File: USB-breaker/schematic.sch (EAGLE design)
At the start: 12 parts, among them K1 G6K-2F-RF, K2 G6K-2F-RF

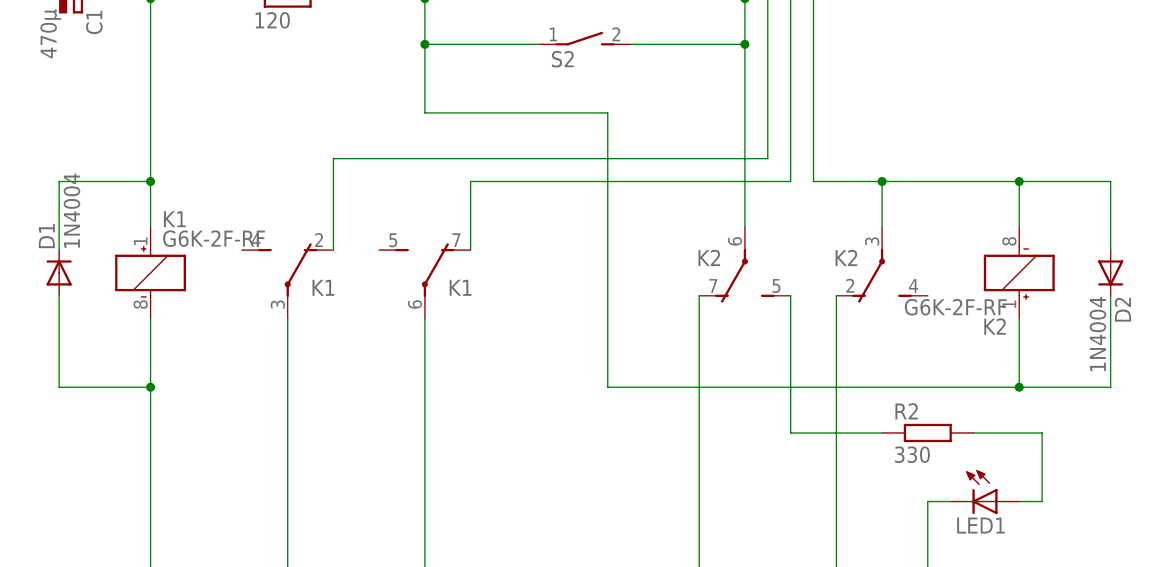
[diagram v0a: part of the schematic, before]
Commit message: Replaced K1 & K2 relay G6K-RF with G6K-2P. SMD --> THT
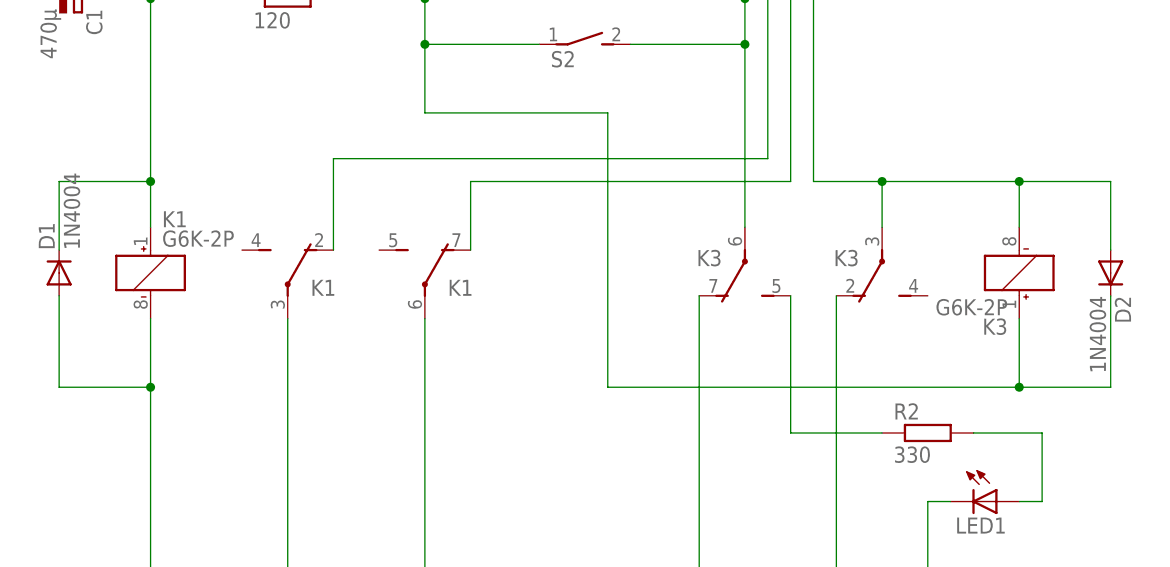
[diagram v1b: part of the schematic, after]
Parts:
- removed K2: G6K-2F-RF, relay:G6K-2F-RF
- added K3: G6K-2P, relay:G6K-2P
- K1: value G6K-2F-RF -> G6K-2P; device relay:G6K-2F-RF -> relay:G6K-2P
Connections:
- net D+-IN: now also K13.O; no longer K1B.O
- net D+-OUT: now also K13.P; no longer K1B.P
- net D--IN: now also K12.O; no longer K1A.O
- net D--OUT: now also K12.P; no longer K1A.P
- net ENABLE: now also K31.+; no longer K21.+
- net GND-IN: now also K31.-, K32.P; no longer K21.-, K2A.P
- net GND-OUT: now also K32.O; no longer K2A.O
- net N$7: now also K33.S; no longer K2B.S
- net VCC-IN: now also K33.P; no longer K2B.P
- net VCC-OUT: now also K33.O; no longer K2B.O
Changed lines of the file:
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@@
 <part name="X1" library="con-berg" deviceset="PN87520" device=""/>
 <part name="X2" library="con-berg" deviceset="PN87520" device=""/>
-<part name="K1" library="relay" deviceset="G6K*-2F-RF" device=""/>
-<part name="K2" library="relay" deviceset="G6K*-2F-RF" device=""/>
 <part name="S1" library="switch-omron" deviceset="31-XX" device=""/>
 <part name="R1" library="resistor" deviceset="R-EU_" device="0207/10" value="120"/>
@@
 <part name="R2" library="resistor" deviceset="R-EU_" device="0207/10" value="330"/>
 <part name="D2" library="diode" deviceset="1N4004" device=""/>
+<part name="K1" library="relay" deviceset="G6K" device="-2P"/>
+<part name="K3" library="relay" deviceset="G6K" device="-2P"/>
 </parts>
 <sheets>
@@
 <instance part="X1" gate="G$1" x="114.3" y="114.3" rot="R90"/>
 <instance part="X2" gate="G$1" x="152.4" y="40.64" rot="MR180"/>
-<instance part="K1" gate="1" x="43.18" y="78.74"/>
-<instance part="K1" gate="A" x="58.42" y="76.2"/>
-<instance part="K1" gate="B" x="73.66" y="76.2"/>
-<instance part="K2" gate="1" x="139.7" y="78.74" rot="R180"/>
-<instance part="K2" gate="A" x="124.46" y="81.28" rot="R180"/>
-<instance part="K2" gate="B" x="109.22" y="81.28" rot="R180"/>
 <instance part="S1" gate="1" x="91.44" y="109.22" rot="R270"/>
 <instance part="R1" gate="G$1" x="58.42" y="109.22"/>
@@
 <instance part="R2" gate="G$1" x="129.54" y="60.96"/>
 <instance part="D2" gate="1" x="149.86" y="78.74" rot="R270"/>
+<instance part="K1" gate="1" x="43.18" y="78.74"/>
+<instance part="K1" gate="2" x="58.42" y="76.2"/>
+<instance part="K1" gate="3" x="73.66" y="76.2"/>
+<instance part="K3" gate="1" x="139.7" y="78.74" rot="R180"/>
+<instance part="K3" gate="2" x="124.46" y="81.28" rot="R180"/>
+<instance part="K3" gate="3" x="109.22" y="81.28" rot="R180"/>
 </instances>
 <busses>
@@
 <wire x1="96.52" y1="109.22" x2="109.22" y2="109.22" width="0.1524" layer="91"/>
 <junction x="109.22" y="109.22"/>
-<pinref part="K2" gate="B" pin="P"/>
 <pinref part="S2" gate="1" pin="2"/>
 <wire x1="96.52" y1="104.14" x2="109.22" y2="104.14" width="0.1524" layer="91"/>
 <junction x="109.22" y="104.14"/>
+<pinref part="K3" gate="3" pin="P"/>
 </segment>
 </net>
@@
 <wire x1="116.84" y1="111.76" x2="116.84" y2="88.9" width="0.1524" layer="91"/>
 <wire x1="116.84" y1="88.9" x2="124.46" y2="88.9" width="0.1524" layer="91"/>
-<pinref part="K2" gate="A" pin="P"/>
 <wire x1="124.46" y1="88.9" x2="124.46" y2="83.82" width="0.1524" layer="91"/>
 <wire x1="124.46" y1="88.9" x2="139.7" y2="88.9" width="0.1524" layer="91"/>
 <junction x="124.46" y="88.9"/>
-<pinref part="K2" gate="1" pin="-"/>
 <wire x1="139.7" y1="88.9" x2="139.7" y2="83.82" width="0.1524" layer="91"/>
 <wire x1="139.7" y1="88.9" x2="149.86" y2="88.9" width="0.1524" layer="91"/>
@@
 <junction x="139.7" y="88.9"/>
 <pinref part="D2" gate="1" pin="A"/>
+<pinref part="K3" gate="1" pin="-"/>
+<pinref part="K3" gate="2" pin="P"/>
 </segment>
 </net>
 <net name="GND-OUT" class="0">
 <segment>
-<pinref part="X2" gate="G$1" pin="4"/>
-<pinref part="K1" gate="1" pin="-"/>
 <wire x1="43.18" y1="73.66" x2="43.18" y2="66.04" width="0.1524" layer="91"/>
 <wire x1="43.18" y1="66.04" x2="43.18" y2="43.18" width="0.1524" layer="91"/>
-<wire x1="43.18" y1="43.18" x2="119.38" y2="43.18" width="0.1524" layer="91"/>
 <pinref part="C1" gate="G$1" pin="-"/>
-<wire x1="119.38" y1="43.18" x2="129.54" y2="43.18" width="0.1524" layer="91"/>
-<wire x1="129.54" y1="43.18" x2="149.86" y2="43.18" width="0.1524" layer="91"/>
 <wire x1="30.48" y1="109.22" x2="25.4" y2="109.22" width="0.1524" layer="91"/>
 <wire x1="25.4" y1="109.22" x2="25.4" y2="43.18" width="0.1524" layer="91"/>
 <wire x1="25.4" y1="43.18" x2="43.18" y2="43.18" width="0.1524" layer="91"/>
-<junction x="43.18" y="43.18"/>
 <pinref part="D1" gate="1" pin="A"/>
 <wire x1="33.02" y1="76.2" x2="33.02" y2="66.04" width="0.1524" layer="91"/>
 <wire x1="33.02" y1="66.04" x2="43.18" y2="66.04" width="0.1524" layer="91"/>
 <junction x="43.18" y="66.04"/>
-<pinref part="K2" gate="A" pin="O"/>
-<wire x1="119.38" y1="76.2" x2="119.38" y2="43.18" width="0.1524" layer="91"/>
-<junction x="119.38" y="43.18"/>
+<pinref part="K1" gate="1" pin="-"/>
+<pinref part="X2" gate="G$1" pin="4"/>
+<wire x1="129.54" y1="43.18" x2="149.86" y2="43.18" width="0.1524" layer="91"/>
 <pinref part="LED1" gate="G$1" pin="C"/>
 <wire x1="132.08" y1="53.34" x2="129.54" y2="53.34" width="0.1524" layer="91"/>
 <wire x1="129.54" y1="53.34" x2="129.54" y2="43.18" width="0.1524" layer="91"/>
 <junction x="129.54" y="43.18"/>
+<wire x1="119.38" y1="43.18" x2="129.54" y2="43.18" width="0.1524" layer="91"/>
+<wire x1="119.38" y1="76.2" x2="119.38" y2="43.18" width="0.1524" layer="91"/>
+<wire x1="43.18" y1="43.18" x2="119.38" y2="43.18" width="0.1524" layer="91"/>
+<junction x="43.18" y="43.18"/>
+<junction x="119.38" y="43.18"/>
+<pinref part="K3" gate="2" pin="O"/>
 </segment>
 </net>
@@
 <pinref part="X2" gate="G$1" pin="1"/>
 <wire x1="104.14" y1="35.56" x2="149.86" y2="35.56" width="0.1524" layer="91"/>
-<pinref part="K2" gate="B" pin="O"/>
 <wire x1="104.14" y1="76.2" x2="104.14" y2="35.56" width="0.1524" layer="91"/>
+<pinref part="K3" gate="3" pin="O"/>
 </segment>
 </net>
@@
 <wire x1="111.76" y1="111.76" x2="111.76" y2="91.44" width="0.1524" layer="91"/>
 <wire x1="111.76" y1="91.44" x2="63.5" y2="91.44" width="0.1524" layer="91"/>
-<pinref part="K1" gate="A" pin="O"/>
+<pinref part="K1" gate="2" pin="O"/>
 <wire x1="63.5" y1="91.44" x2="63.5" y2="81.28" width="0.1524" layer="91"/>
 </segment>
@@
 <wire x1="114.3" y1="111.76" x2="114.3" y2="88.9" width="0.1524" layer="91"/>
 <wire x1="114.3" y1="88.9" x2="78.74" y2="88.9" width="0.1524" layer="91"/>
-<pinref part="K1" gate="B" pin="O"/>
+<pinref part="K1" gate="3" pin="O"/>
 <wire x1="78.74" y1="88.9" x2="78.74" y2="81.28" width="0.1524" layer="91"/>
 </segment>
@@
 <net name="D+-OUT" class="0">
 <segment>
-<pinref part="K1" gate="B" pin="P"/>
 <pinref part="X2" gate="G$1" pin="3"/>
+<wire x1="73.66" y1="40.64" x2="149.86" y2="40.64" width="0.1524" layer="91"/>
+<pinref part="K1" gate="3" pin="P"/>
 <wire x1="73.66" y1="73.66" x2="73.66" y2="40.64" width="0.1524" layer="91"/>
-<wire x1="73.66" y1="40.64" x2="149.86" y2="40.64" width="0.1524" layer="91"/>
 </segment>
 </net>
 <net name="D--OUT" class="0">
 <segment>
-<pinref part="K1" gate="A" pin="P"/>
 <pinref part="X2" gate="G$1" pin="2"/>
+<wire x1="58.42" y1="38.1" x2="149.86" y2="38.1" width="0.1524" layer="91"/>
+<pinref part="K1" gate="2" pin="P"/>
 <wire x1="58.42" y1="73.66" x2="58.42" y2="38.1" width="0.1524" layer="91"/>
-<wire x1="58.42" y1="38.1" x2="149.86" y2="38.1" width="0.1524" layer="91"/>
 </segment>
 </net>
@@
 <pinref part="C1" gate="G$1" pin="+"/>
 <wire x1="53.34" y1="109.22" x2="43.18" y2="109.22" width="0.1524" layer="91"/>
-<pinref part="K1" gate="1" pin="+"/>
 <wire x1="43.18" y1="109.22" x2="38.1" y2="109.22" width="0.1524" layer="91"/>
 <wire x1="43.18" y1="83.82" x2="43.18" y2="88.9" width="0.1524" layer="91"/>
@@
 <pinref part="D1" gate="1" pin="C"/>
 <wire x1="33.02" y1="88.9" x2="33.02" y2="81.28" width="0.1524" layer="91"/>
+<pinref part="K1" gate="1" pin="+"/>
 </segment>
 </net>
@@
 <wire x1="93.98" y1="96.52" x2="93.98" y2="66.04" width="0.1524" layer="91"/>
 <wire x1="93.98" y1="66.04" x2="139.7" y2="66.04" width="0.1524" layer="91"/>
-<pinref part="K2" gate="1" pin="+"/>
 <wire x1="139.7" y1="66.04" x2="139.7" y2="73.66" width="0.1524" layer="91"/>
 <pinref part="S2" gate="1" pin="1"/>
@@
 <wire x1="149.86" y1="66.04" x2="139.7" y2="66.04" width="0.1524" layer="91"/>
 <junction x="139.7" y="66.04"/>
+<pinref part="K3" gate="1" pin="+"/>
 </segment>
 </net>
@@
 <net name="N$7" class="0">
 <segment>
-<pinref part="K2" gate="B" pin="S"/>
 <wire x1="114.3" y1="76.2" x2="114.3" y2="60.96" width="0.1524" layer="91"/>
 <pinref part="R2" gate="G$1" pin="1"/>
 <wire x1="114.3" y1="60.96" x2="124.46" y2="60.96" width="0.1524" layer="91"/>
+<pinref part="K3" gate="3" pin="S"/>
 </segment>
 </net>

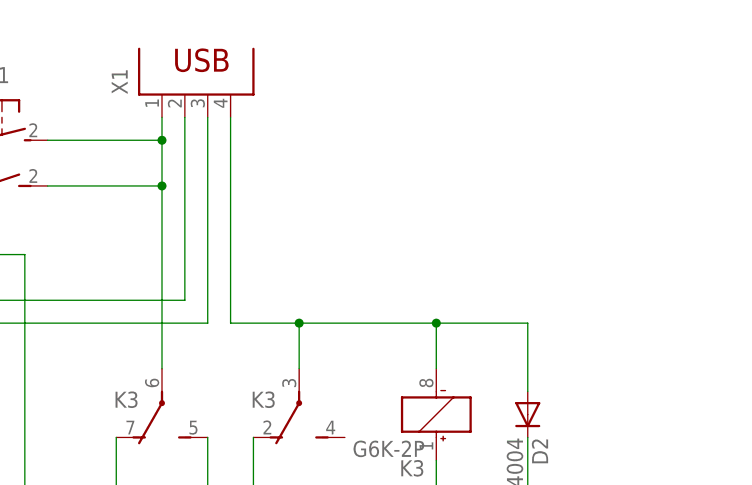
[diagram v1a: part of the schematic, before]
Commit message: Added a Mini USB and Micro USB input connector.
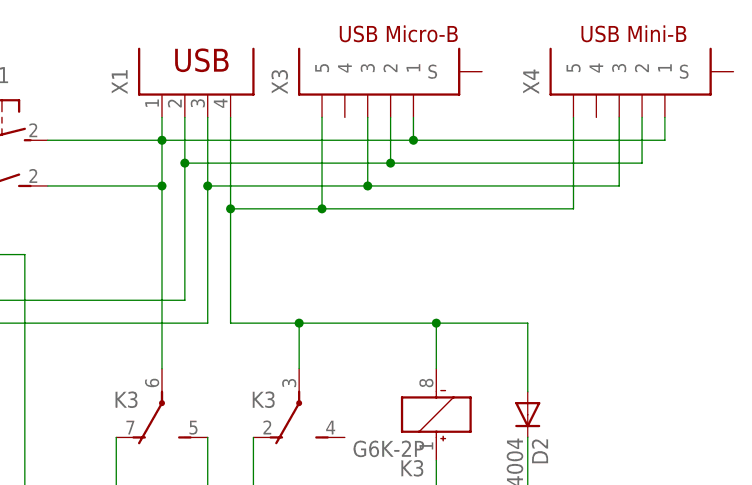
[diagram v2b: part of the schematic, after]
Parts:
- added X3: (no value), mibe:10104110
- added X4: (no value), mibe:UX60SC-MB-5ST
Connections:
- net D+-IN: now also X3.3, X4.3
- net D--IN: now also X3.2, X4.2
- net GND-IN: now also X3.5, X4.5
- net VCC-IN: now also X3.1, X4.1
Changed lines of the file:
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@@
 <setting verticaltext="up"/>
 </settings>
-<grid distance="0.1" unitdist="inch" unit="inch" style="lines" multiple="1" display="yes" altdistance="0.01" altunitdist="inch" altunit="inch"/>
+<grid distance="0.1" unitdist="inch" unit="inch" style="lines" multiple="1" display="no" altdistance="0.01" altunitdist="inch" altunit="inch"/>
 <layers>
 <layer number="1" name="Top" color="4" fill="1" visible="no" active="no"/>
@@
 <part name="K1" library="relay" deviceset="G6K" device="-2P"/>
 <part name="K3" library="relay" deviceset="G6K" device="-2P"/>
+<part name="X3" library="mibe" deviceset="10104110" device=""/>
+<part name="X4" library="mibe" deviceset="UX60S" device="C-MB-5ST"/>
 </parts>
 <sheets>
@@
 <instance part="K3" gate="2" x="124.46" y="81.28" rot="R180"/>
 <instance part="K3" gate="3" x="109.22" y="81.28" rot="R180"/>
+<instance part="X3" gate="G$1" x="137.16" y="121.92" rot="R90"/>
+<instance part="X4" gate="G$1" x="165.1" y="121.92" rot="R90"/>
 </instances>
 <busses>
@@
 <junction x="109.22" y="104.14"/>
 <pinref part="K3" gate="3" pin="P"/>
+<pinref part="X3" gate="G$1" pin="1"/>
+<wire x1="109.22" y1="109.22" x2="137.16" y2="109.22" width="0.1524" layer="91"/>
+<wire x1="137.16" y1="109.22" x2="137.16" y2="111.76" width="0.1524" layer="91"/>
+<pinref part="X4" gate="G$1" pin="1"/>
+<wire x1="137.16" y1="109.22" x2="165.1" y2="109.22" width="0.1524" layer="91"/>
+<wire x1="165.1" y1="109.22" x2="165.1" y2="111.76" width="0.1524" layer="91"/>
+<junction x="137.16" y="109.22"/>
 </segment>
 </net>
@@
 <segment>
 <pinref part="X1" gate="G$1" pin="4"/>
-<wire x1="116.84" y1="111.76" x2="116.84" y2="88.9" width="0.1524" layer="91"/>
+<wire x1="116.84" y1="111.76" x2="116.84" y2="101.6" width="0.1524" layer="91"/>
+<wire x1="116.84" y1="101.6" x2="116.84" y2="88.9" width="0.1524" layer="91"/>
 <wire x1="116.84" y1="88.9" x2="124.46" y2="88.9" width="0.1524" layer="91"/>
 <wire x1="124.46" y1="88.9" x2="124.46" y2="83.82" width="0.1524" layer="91"/>
@@
 <pinref part="K3" gate="1" pin="-"/>
 <pinref part="K3" gate="2" pin="P"/>
+<pinref part="X3" gate="G$1" pin="5"/>
+<wire x1="116.84" y1="101.6" x2="127" y2="101.6" width="0.1524" layer="91"/>
+<wire x1="127" y1="101.6" x2="127" y2="111.76" width="0.1524" layer="91"/>
+<junction x="116.84" y="101.6"/>
+<pinref part="X4" gate="G$1" pin="5"/>
+<wire x1="127" y1="101.6" x2="154.94" y2="101.6" width="0.1524" layer="91"/>
+<wire x1="154.94" y1="101.6" x2="154.94" y2="111.76" width="0.1524" layer="91"/>
+<junction x="127" y="101.6"/>
 </segment>
 </net>
@@
 <segment>
 <pinref part="X1" gate="G$1" pin="2"/>
-<wire x1="111.76" y1="111.76" x2="111.76" y2="91.44" width="0.1524" layer="91"/>
+<wire x1="111.76" y1="111.76" x2="111.76" y2="106.68" width="0.1524" layer="91"/>
+<wire x1="111.76" y1="106.68" x2="111.76" y2="91.44" width="0.1524" layer="91"/>
 <wire x1="111.76" y1="91.44" x2="63.5" y2="91.44" width="0.1524" layer="91"/>
 <pinref part="K1" gate="2" pin="O"/>
 <wire x1="63.5" y1="91.44" x2="63.5" y2="81.28" width="0.1524" layer="91"/>
+<pinref part="X3" gate="G$1" pin="2"/>
+<wire x1="111.76" y1="106.68" x2="134.62" y2="106.68" width="0.1524" layer="91"/>
+<wire x1="134.62" y1="106.68" x2="134.62" y2="111.76" width="0.1524" layer="91"/>
+<junction x="111.76" y="106.68"/>
+<pinref part="X4" gate="G$1" pin="2"/>
+<wire x1="134.62" y1="106.68" x2="162.56" y2="106.68" width="0.1524" layer="91"/>
+<wire x1="162.56" y1="106.68" x2="162.56" y2="111.76" width="0.1524" layer="91"/>
+<junction x="134.62" y="106.68"/>
 </segment>
 </net>
@@
 <segment>
 <pinref part="X1" gate="G$1" pin="3"/>
-<wire x1="114.3" y1="111.76" x2="114.3" y2="88.9" width="0.1524" layer="91"/>
+<wire x1="114.3" y1="111.76" x2="114.3" y2="104.14" width="0.1524" layer="91"/>
+<wire x1="114.3" y1="104.14" x2="114.3" y2="88.9" width="0.1524" layer="91"/>
 <wire x1="114.3" y1="88.9" x2="78.74" y2="88.9" width="0.1524" layer="91"/>
 <pinref part="K1" gate="3" pin="O"/>
 <wire x1="78.74" y1="88.9" x2="78.74" y2="81.28" width="0.1524" layer="91"/>
-</segment>
-</net>
+<pinref part="X3" gate="G$1" pin="3"/>
+<wire x1="114.3" y1="104.14" x2="132.08" y2="104.14" width="0.1524" layer="91"/>
+<wire x1="132.08" y1="104.14" x2="132.08" y2="111.76" width="0.1524" layer="91"/>
+<junction x="114.3" y="104.14"/>
+<pinref part="X4" gate="G$1" pin="3"/>
+<wire x1="132.08" y1="104.14" x2="160.02" y2="104.14" width="0.1524" layer="91"/>
+<wire x1="160.02" y1="104.14" x2="160.02" y2="111.76" width="0.1524" layer="91"/>
+<junction x="132.08" y="104.14"/>
+</segment>
+</net>
